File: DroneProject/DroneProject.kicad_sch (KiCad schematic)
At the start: 0 parts

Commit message: Initial Prototype Schematic for testing MCU and various sensors complete
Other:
- added sheet Connectors (Connectors.kicad_sch)
- added sheet Debug (Debug.kicad_sch)
- added sheet MCU (MCU.kicad_sch)
- added sheet Peripherals (Sensors.kicad_sch)
- added sheet Power (Power.kicad_sch)
- added sheet Transciever (Transciever.kicad_sch)
- title: (none) -> DroneProject

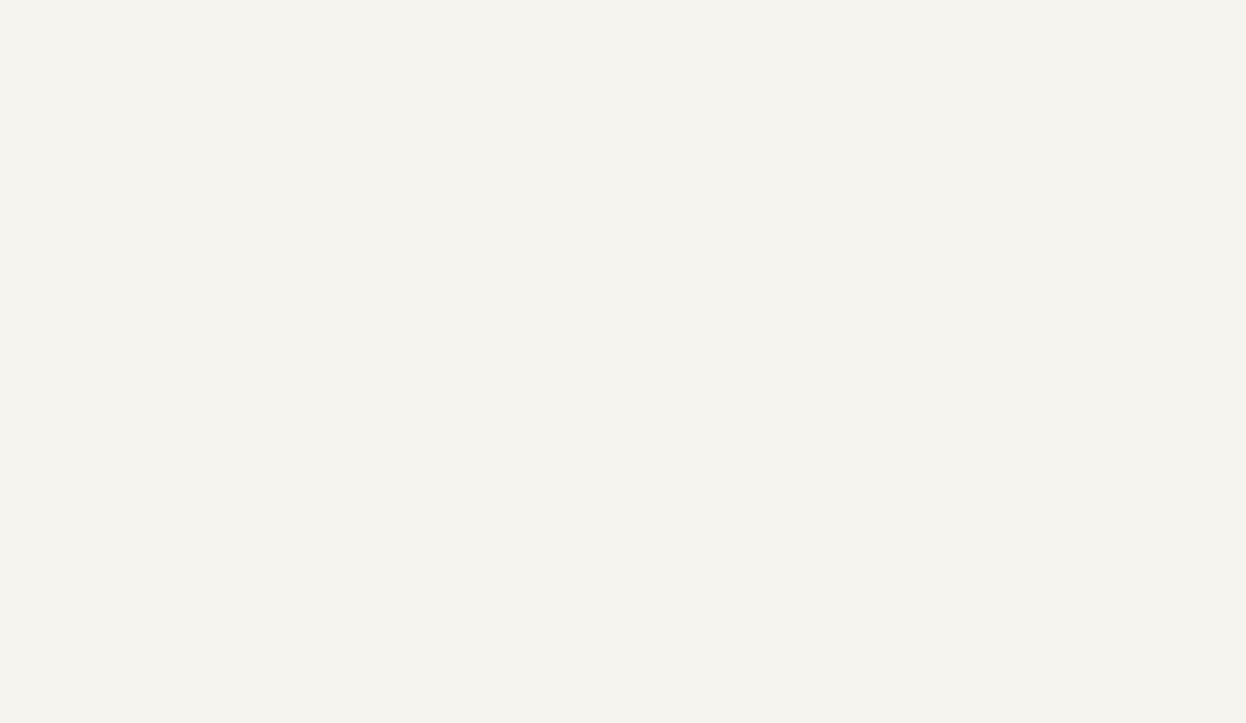
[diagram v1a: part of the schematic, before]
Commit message: Added mounting holes and some more testpoints.  Also started on PCB with dimesions and mounting holes measured and placed
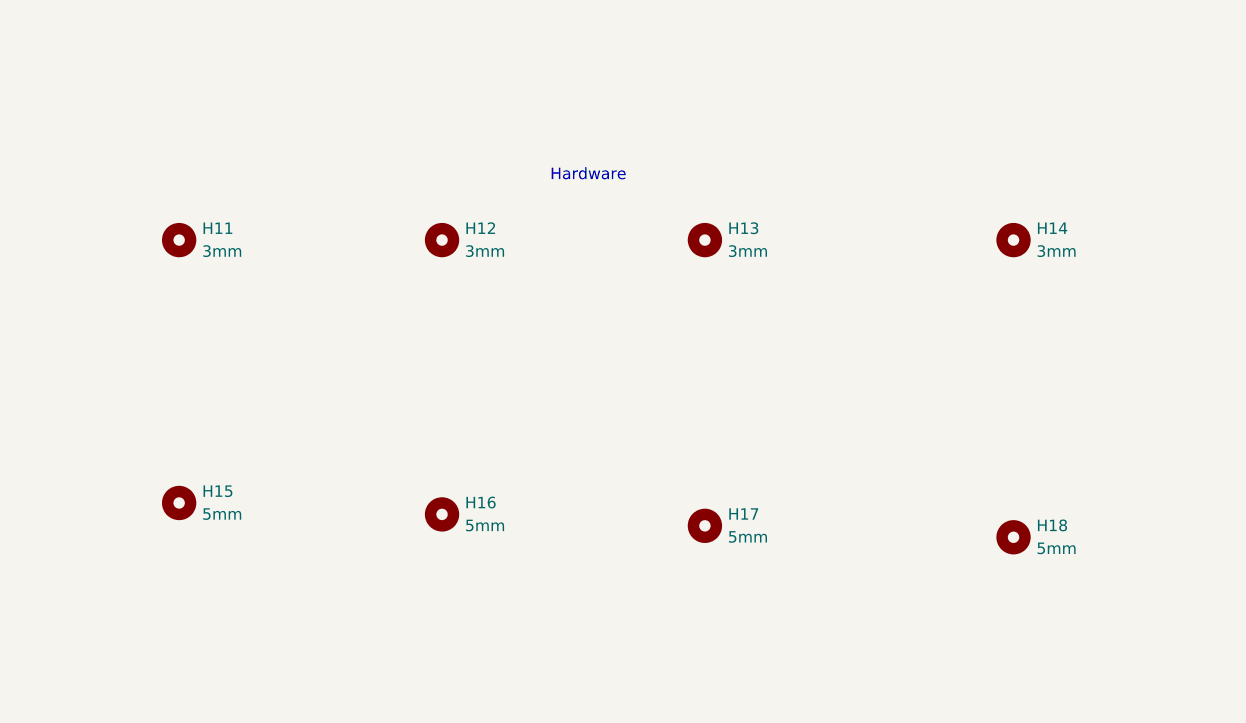
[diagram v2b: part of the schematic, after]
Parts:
- added H11, H12, H13, H14: 3mm, MountingHole:MountingHole_3mm, symbol Mechanical:MountingHole
- added H15, H16, H17, H18: 5mm, MountingHole:MountingHole_5mm, symbol Mechanical:MountingHole
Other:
- note added: "Hardware"

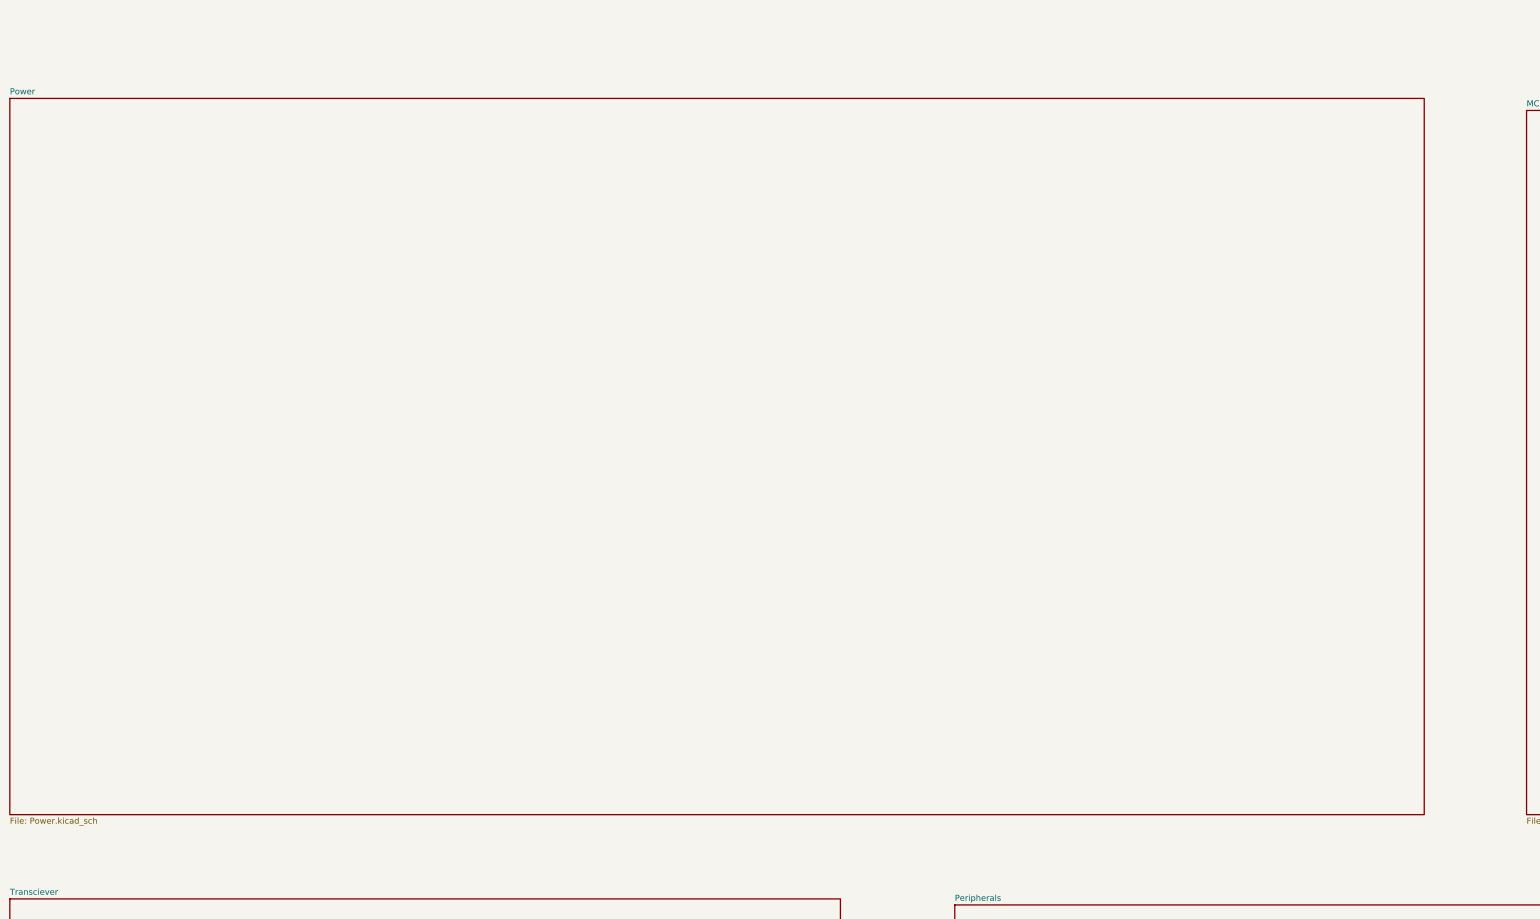
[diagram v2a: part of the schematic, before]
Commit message: Finished initial PCB layout.  However decided to go ahead and add the motor drivers for the first prototype anyways.  Re-did the reverse-polarity detection to use an NMOS instead of a PMOS.  Added sheets for each motor, still need to decide on parts.
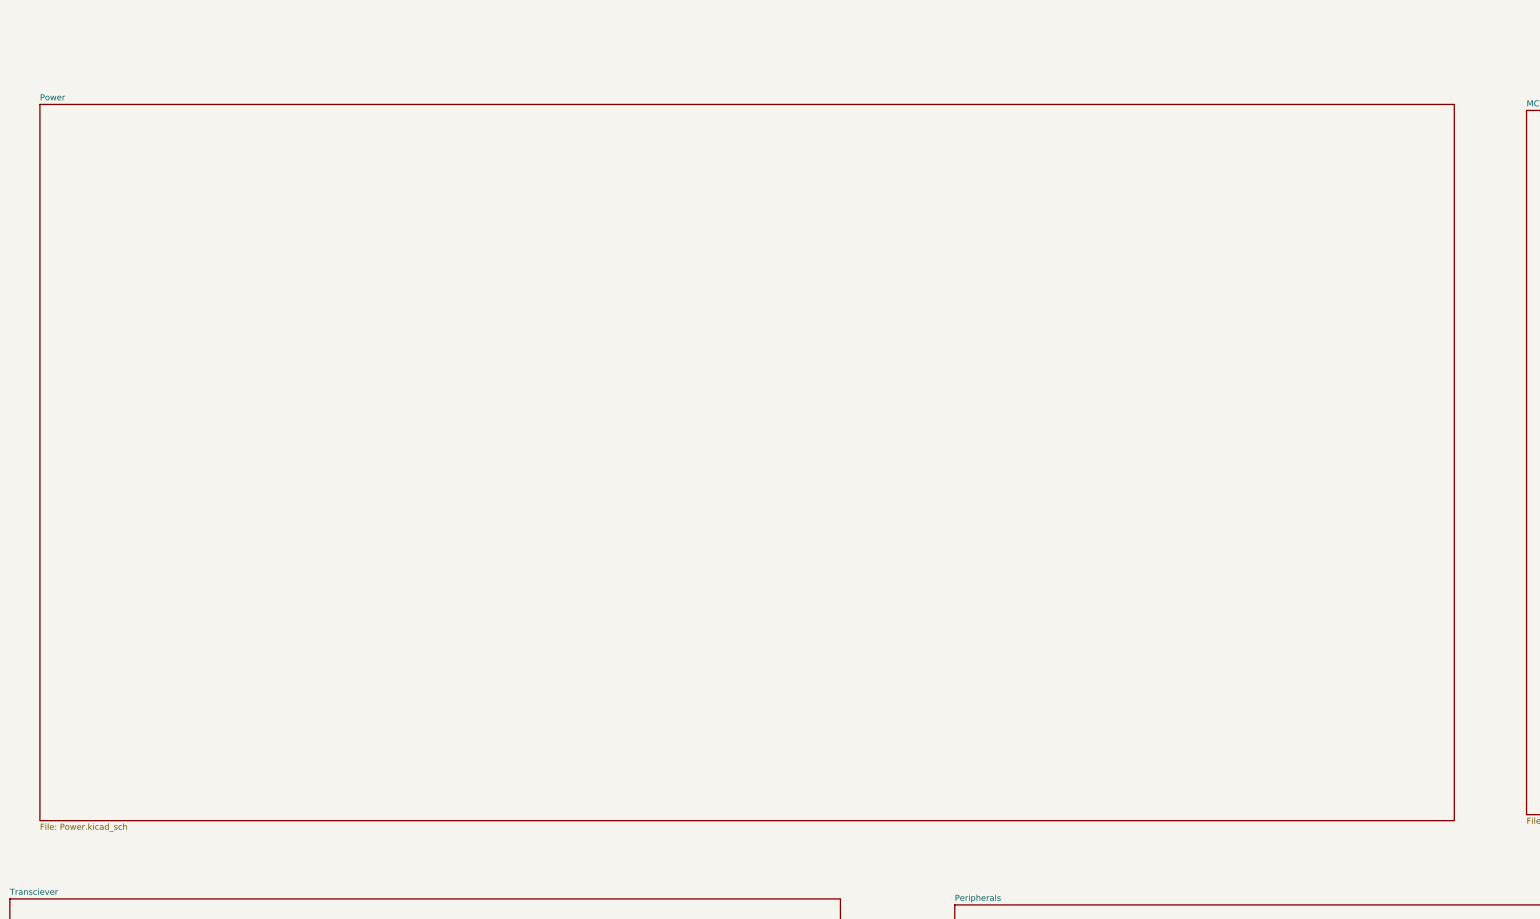
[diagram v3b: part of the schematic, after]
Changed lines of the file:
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@@
 	)
 	(sheet
-		(at 0 236.22)
+		(at 6.35 237.49)
 		(size 298.45 151.13)
 		(exclude_from_sim no)
@@
 		)
 		(property "Sheetname" "Power"
-			(at 0 235.5084 0)
+			(at 6.35 236.7784 0)
 			(effects
 				(font
@@
 		)
 		(property "Sheetfile" "Power.kicad_sch"
-			(at 0 387.9346 0)
+			(at 6.35 389.2046 0)
 			(effects
 				(font

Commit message: Re-did layout for new power system
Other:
- added sheet Motor_1 (Motor_1.kicad_sch)
- added sheet Motor_2 (Motor_2.kicad_sch)
- added sheet Motor_3 (Motor_3.kicad_sch)
- added sheet Motor_4 (Motor_4.kicad_sch)
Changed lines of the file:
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@@
+	)
+	(sheet
+		(at 556.26 575.31)
+		(size 175.26 152.4)
+		(exclude_from_sim no)
+		(in_bom yes)
+		(on_board yes)
+		(dnp no)
+		(fields_autoplaced yes)
+		(stroke
+			(width 0.1524)
+			(type solid)
+		)
+		(fill
+			(color 0 0 0 0.0000)
+		)
+		(property "Sheetname" "Motor_4"
+			(at 556.26 574.5984 0)
+			(effects
+				(font
+					(size 1.27 1.27)
+				)
+				(justify left bottom)
+			)
+		)
+		(property "Sheetfile" "Motor_4.kicad_sch"
+			(at 556.26 728.2946 0)
+			(effects
+				(font
+					(size 1.27 1.27)
+				)
+				(justify left top)
+			)
+		)
+		(instances
+			(project "DroneProject"
+				(path "/feb4ca7b-5376-4689-a73b-f56020a5aa30"
+					(page "11")
+				)
+			)
+		)
 	)
 	(sheet
@@
 				)
 			)
+		)
+	)
+	(sheet
+		(at 0 574.04)
+		(size 179.07 156.21)
+		(exclude_from_sim no)
+		(in_bom yes)
+		(on_board yes)
+		(dnp no)
+		(fields_autoplaced yes)
+		(stroke
+			(width 0.1524)
+			(type solid)
+		)
+		(fill
+			(color 0 0 0 0.0000)
+		)
+		(property "Sheetname" "Motor_1"
+			(at 0 573.3284 0)
+			(effects
+				(font
+					(size 1.27 1.27)
+				)
+				(justify left bottom)
+			)
+		)
+		(property "Sheetfile" "Motor_1.kicad_sch"
+			(at 0 730.8346 0)
+			(effects
+				(font
+					(size 1.27 1.27)
+				)
+				(justify left top)
+			)
+		)
+		(instances
+			(project "DroneProject"
+				(path "/feb4ca7b-5376-4689-a73b-f56020a5aa30"
+					(page "8")
+				)
+			)
+		)
+	)
+	(sheet
+		(at 187.96 575.31)
+		(size 168.91 154.94)
+		(exclude_from_sim no)
+		(in_bom yes)
+		(on_board yes)
+		(dnp no)
+		(fields_autoplaced yes)
+		(stroke
+			(width 0.1524)
+			(type solid)
+		)
+		(fill
+			(color 0 0 0 0.0000)
+		)
+		(property "Sheetname" "Motor_2"
+			(at 187.96 574.5984 0)
+			(effects
+				(font
+					(size 1.27 1.27)
+				)
+				(justify left bottom)
+			)
+		)
+		(property "Sheetfile" "Motor_2.kicad_sch"
+			(at 187.96 730.8346 0)
+			(effects
+				(font
+					(size 1.27 1.27)
+				)
+				(justify left top)
+			)
+		)
+		(instances
+			(project "DroneProject"
+				(path "/feb4ca7b-5376-4689-a73b-f56020a5aa30"
+					(page "9")
+				)
+			)
+		)
+	)
+	(sheet
+		(at 372.11 575.31)
+		(size 166.37 153.67)
+		(exclude_from_sim no)
+		(in_bom yes)
+		(on_board yes)
+		(dnp no)
+		(fields_autoplaced yes)
+		(stroke
+			(width 0.1524)
+			(type solid)
+		)
+		(fill
+			(color 0 0 0 0.0000)
+		)
+		(property "Sheetname" "Motor_3"
+			(at 372.11 574.5984 0)
+			(effects
+				(font
+					(size 1.27 1.27)
+				)
+				(justify left bottom)
+			)
+		)
+		(property "Sheetfile" "Motor_3.kicad_sch"
+			(at 372.11 729.5646 0)
+			(effects
+				(font
+					(size 1.27 1.27)
+				)
+				(justify left top)
+			)
+		)
+		(instances
+			(project "DroneProject"
+				(path "/feb4ca7b-5376-4689-a73b-f56020a5aa30"
+					(page "10")
+				)
+			)

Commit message: Added a second MCU for motor control.  Removed 5V rail.  Added COM switching for SWD and UART external headers
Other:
- added sheet Motor Controller (Motor_Control.kicad_sch)
- added sheet Prog (Prog.kicad_sch)
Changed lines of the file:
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@@
 	)
 	(sheet
-		(at 389.89 406.4)
+		(at 363.22 406.4)
 		(size 194.31 160.02)
 		(exclude_from_sim no)
@@
 		)
 		(property "Sheetname" "Debug"
-			(at 389.89 405.6884 0)
+			(at 363.22 405.6884 0)
 			(effects
 				(font
@@
 		)
 		(property "Sheetfile" "Debug.kicad_sch"
-			(at 389.89 567.0046 0)
+			(at 363.22 567.0046 0)
 			(effects
 				(font
@@
 			(project "DroneProject"
 				(path "/feb4ca7b-5376-4689-a73b-f56020a5aa30"
-					(page "11")
-				)
-			)
-		)
-	)
-	(sheet
-		(at 199.39 406.4)
+					(page "12")
+				)
+			)
+		)
+	)
+	(sheet
+		(at 189.23 406.4)
 		(size 161.29 160.02)
 		(exclude_from_sim no)
@@
 		)
 		(property "Sheetname" "Peripherals"
-			(at 199.39 405.6884 0)
+			(at 189.23 405.6884 0)
 			(effects
 				(font
@@
 		)
 		(property "Sheetfile" "Sensors.kicad_sch"
-			(at 199.39 567.0046 0)
+			(at 189.23 567.0046 0)
 			(effects
 				(font
@@
 			(project "DroneProject"
 				(path "/feb4ca7b-5376-4689-a73b-f56020a5aa30"
-					(page "8")
+					(page "9")
 				)
 			)
@@
 			(project "DroneProject"
 				(path "/feb4ca7b-5376-4689-a73b-f56020a5aa30"
-					(page "9")
+					(page "10")
+				)
+			)
+		)
+	)
+	(sheet
+		(at 575.31 407.67)
+		(size 226.06 157.48)
+		(exclude_from_sim no)
+		(in_bom yes)
+		(on_board yes)
+		(dnp no)
+		(fields_autoplaced yes)
+		(stroke
+			(width 0.1524)
+			(type solid)
+		)
+		(fill
+			(color 0 0 0 0.0000)
+		)
+		(property "Sheetname" "Motor Controller"
+			(at 575.31 406.9584 0)
+			(effects
+				(font
+					(size 1.27 1.27)
+				)
+				(justify left bottom)
+			)
+		)
+		(property "Sheetfile" "Motor_Control.kicad_sch"
+			(at 575.31 565.7346 0)
+			(effects
+				(font
+					(size 1.27 1.27)
+				)
+				(justify left top)
+			)
+		)
+		(instances
+			(project "DroneProject"
+				(path "/feb4ca7b-5376-4689-a73b-f56020a5aa30"
+					(page "8")
+				)
+			)
+		)
+	)
+	(sheet
+		(at 601.98 238.76)
+		(size 195.58 144.78)
+		(exclude_from_sim no)
+		(in_bom yes)
+		(on_board yes)
+		(dnp no)
+		(fields_autoplaced yes)
+		(stroke
+			(width 0.1524)
+			(type solid)
+		)
+		(fill
+			(color 0 0 0 0.0000)
+		)
+		(property "Sheetname" "Prog"
+			(at 601.98 238.0484 0)
+			(effects
+				(font
+					(size 1.27 1.27)
+				)
+				(justify left bottom)
+			)
+		)
+		(property "Sheetfile" "Prog.kicad_sch"
+			(at 601.98 384.1246 0)
+			(effects
+				(font
+					(size 1.27 1.27)
+				)
+				(justify left top)
+			)
+		)
+		(instances
+			(project "DroneProject"
+				(path "/feb4ca7b-5376-4689-a73b-f56020a5aa30"
+					(page "13")
 				)
 			)
@@
 			(project "DroneProject"
 				(path "/feb4ca7b-5376-4689-a73b-f56020a5aa30"
-					(page "10")
-				)
-			)
+					(page "11")
+				)
+			)

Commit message: Removed C1 and motor controllers from main platform and moved to own project
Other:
- removed sheet Motor Controller
- removed sheet Motor_1
- removed sheet Motor_2
- removed sheet Motor_3
- removed sheet Motor_4
- removed sheet Prog
